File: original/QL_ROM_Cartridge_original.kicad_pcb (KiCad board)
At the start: 2 copper layers, 39.4 x 86.4 mm, 6 parts, among them IC1 27C128, IC2 27C128, IC3 74LS00, J1 QL_cartridge_ROM

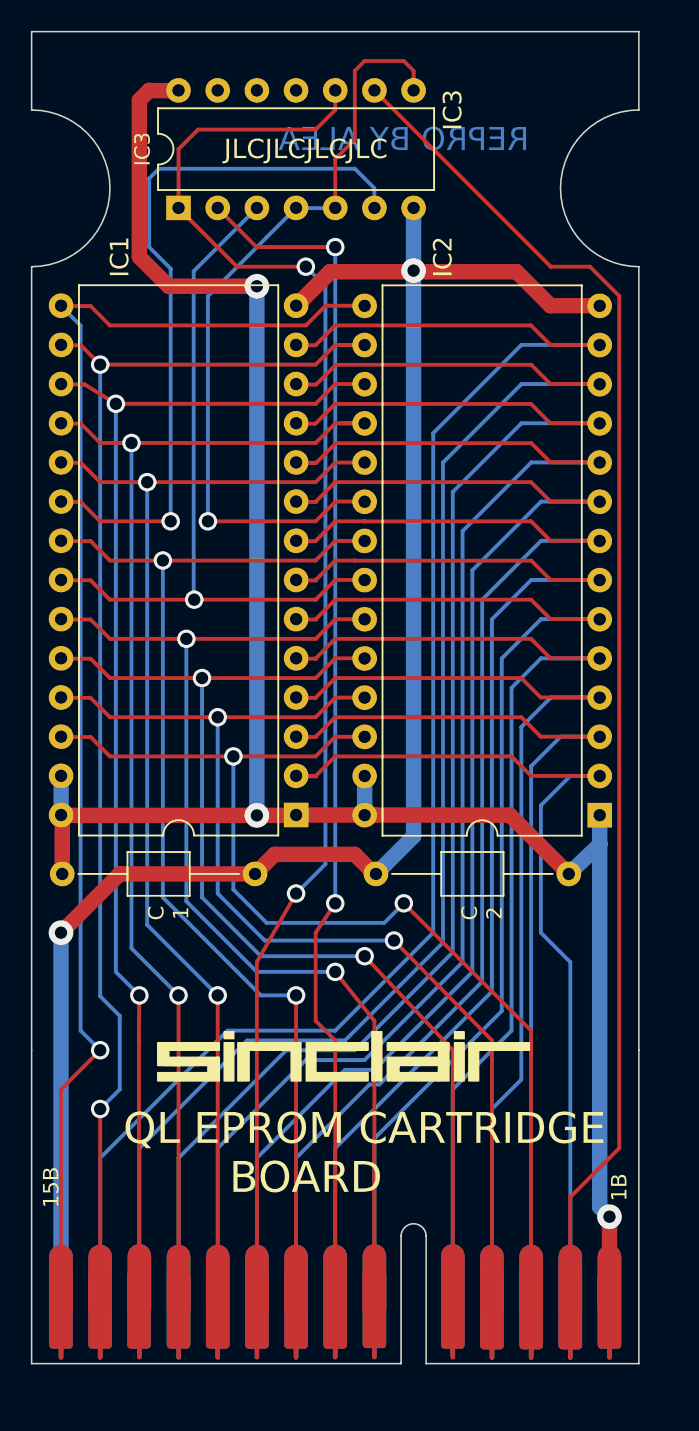
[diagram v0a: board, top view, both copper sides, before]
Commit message: Update size after feedback
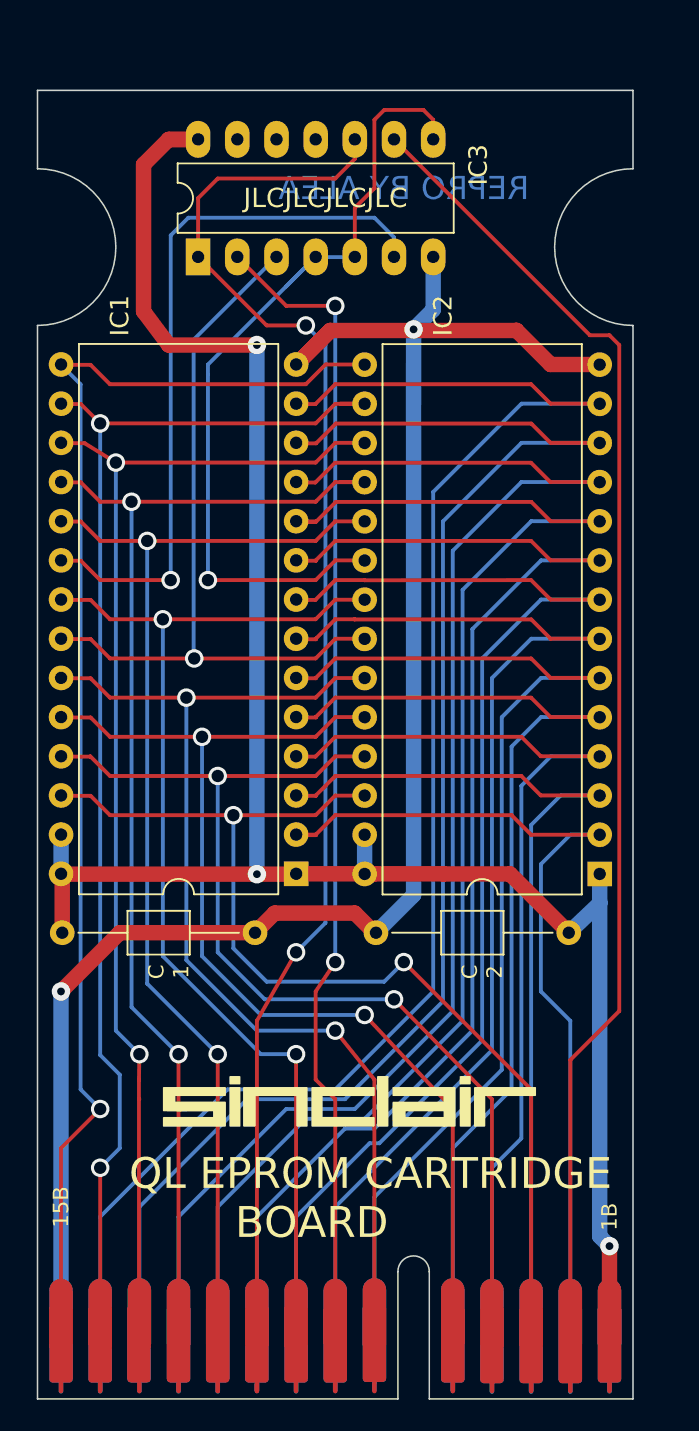
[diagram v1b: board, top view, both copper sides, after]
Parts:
- IC3: footprint Package_DIP:DIP-14_W7.62mm -> Package_DIP:DIP-14_W7.62mm_LongPads
- moved C1 3.81 mm to (63.6, 114.3)
- moved C2 3.81 mm to (96.4, 114.3)
- moved IC1 3.81 mm to (78.7, 110.5)
- moved IC2 3.81 mm to (98.4, 110.5)
- moved IC3 3.42 mm to (72.4, 70.5)
- moved J1 2.20 mm to (73.7, 140.0)
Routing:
- net /ROMOE: track 76.8 -> 71.9 mm
- net /A14: track 86.7 -> 82.3 mm
- net /A15: track 94.0 -> 89.7 mm
- net /U2_CE: track 49.9 -> 53.7 mm
- net /D0: track 93.4 -> 89.6 mm
- net /A5: track 67.4 -> 63.6 mm
- net /A2: track 79.6 -> 75.8 mm
- net /D4: track 82.3 -> 78.5 mm
- net /D1: track 98.0 -> 94.2 mm
- net /A4: track 72.1 -> 68.2 mm
- net /A3: track 76.1 -> 72.3 mm
- net /D2: track 102.1 -> 98.2 mm
- net /A1: track 84.0 -> 80.2 mm
- net /A0: track 90.3 -> 86.5 mm
- net /A6: track 63.5 -> 59.7 mm
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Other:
- board size 39.4 x 86.4 mm -> 38.6 x 84.8 mm
